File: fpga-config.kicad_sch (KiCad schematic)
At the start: 35 parts, among them J1 PinHeader_2x7_P2mm_SMD_Shroud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, Q1 BSS138PW, Q2 BSS138PW, Q3 BSS138PW, SW1 CVS-03B, SW2 SW_KMR211NGLFS_SMD, U2 TPD4E05U06QDQARQ1, U30 REF3012AIDBZT, U34 XCAU25P-2FFVB676I, U35 TMP451AIDQFR

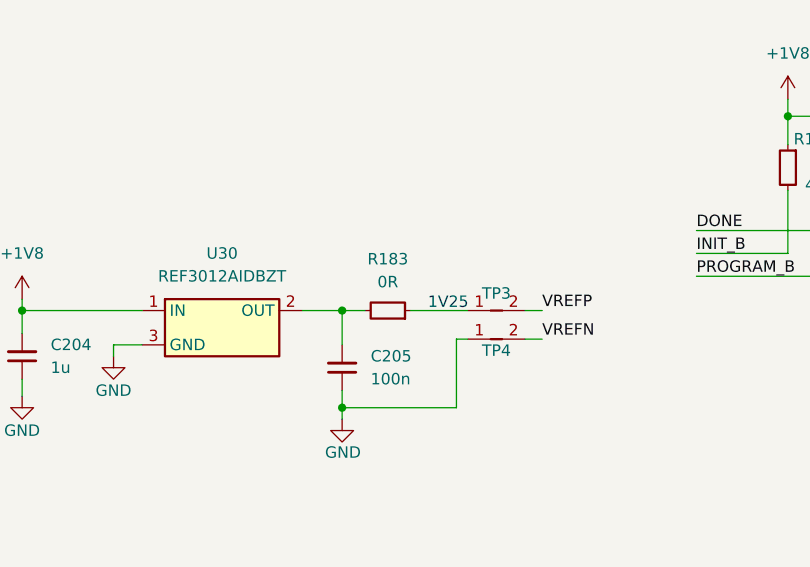
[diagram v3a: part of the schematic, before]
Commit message: [#66727] Route VCCINT sense. Route VREF. Place supply power meters circuits
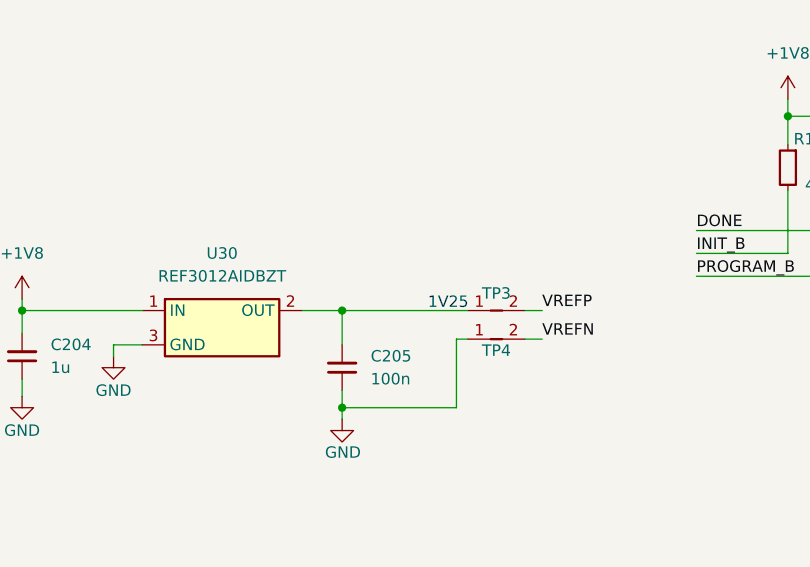
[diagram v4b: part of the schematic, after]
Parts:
- removed R183: R_0R_0402, antmicro-footprints:R_0402_1005Metric, symbol antmicroResistors0402:R_0R_0402
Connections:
- net at TP3.1: now also C205.2, U30.2 (OUT)
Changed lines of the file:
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@@
     (stroke (width 0) (type default))
   )
-  (wire (pts (xy 128.905 83.82) (xy 135.255 83.82))
+  (wire (pts (xy 121.285 83.82) (xy 135.255 83.82))
     (stroke (width 0) (type default))
   )
@@
     (stroke (width 0) (type default))
   )
-  (wire (pts (xy 121.285 83.82) (xy 123.825 83.82))
-    (stroke (width 0) (type default))
-  )
   (wire (pts (xy 29.21 229.87) (xy 29.21 232.41))
     (stroke (width 0) (type default))
@@
         )
       )
-    )
-  )
-  (symbol (lib_name "R_0R_0402_1") (lib_id "antmicroResistors0402:R_0R_0402") (at 128.905 83.82 180) (unit 1)
-    (in_bom yes) (on_board yes) (dnp no) (fields_autoplaced)
-    (property "Reference" "R183" (at 126.365 78.105 0)
-      (effects (font (size 1.27 1.27) (thickness 0.15)))
-    )
-    (property "Value" "R_0R_0402" (at 108.585 71.12 0)
-      (effects (font (size 1.27 1.27) (thickness 0.15)) (justify left bottom) hide)
-    )
-    (property "Footprint" "antmicro-footprints:R_0402_1005Metric" (at 108.585 68.58 0)
-      (effects (font (size 1.27 1.27) (thickness 0.15)) (justify left bottom) hide)
-    )
-    (property "Datasheet" "https://industrial.panasonic.com/cdbs/www-data/pdf/RDA0000/AOA0000C301.pdf" (at 108.585 66.04 0)
-      (effects (font (size 1.27 1.27) (thickness 0.15)) (justify left bottom) hide)
-    )
-    (property "MPN" "ERJ2GE0R00X" (at 108.585 63.5 0)
-      (effects (font (size 1.27 1.27) (thickness 0.15)) (justify left bottom) hide)
-    )
-    (property "Manufacturer" "Panasonic" (at 108.585 60.96 0)
-      (effects (font (size 1.27 1.27) (thickness 0.15)) (justify left bottom) hide)
-    )
-    (property "License" "Apache-2.0" (at 108.585 58.42 0)
-      (effects (font (size 1.27 1.27) (thickness 0.15)) (justify left bottom) hide)
-    )
-    (property "Author" "Antmicro" (at 108.585 55.88 0)
-      (effects (font (size 1.27 1.27) (thickness 0.15)) (justify left bottom) hide)
-    )
-    (property "Val" "0R" (at 126.365 80.645 0)
-      (effects (font (size 1.27 1.27) (thickness 0.15)))
-    )
-    (property "Tolerance" "~" (at 108.585 73.66 0)
-      (effects (font (size 1.27 1.27)) (justify left bottom) hide)
-    )
-    (property "Current" "1A" (at 108.585 53.34 0)
-      (effects (font (size 1.27 1.27) (thickness 0.15)) (justify left bottom) hide)
-    )
-    (pin "1")
-    (pin "2")
-    (instances
-      (project "data-center-rdimm-ddr5-tester"
-        (path "/1faa6543-e26a-4449-8bac-ee14b9f19e5f/00000000-0000-0000-0000-00005fd53c7d"
-          (reference "R183") (unit 1)
-        )
-      )

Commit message: [#66727] Continue routing low speed signals
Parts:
- R18: footprint antmicro-footprints:R_0402_1005Metric -> antmicro-footprints:R_0402_1005Metric_EIA
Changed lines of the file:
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@@
       (effects (font (size 1.27 1.27) (thickness 0.15)) (justify left bottom) hide)
     )
-    (property "Footprint" "antmicro-footprints:R_0402_1005Metric" (at 163.83 85.725 0)
+    (property "Footprint" "antmicro-footprints:R_0402_1005Metric_EIA" (at 163.83 85.725 0)
       (effects (font (size 1.27 1.27) (thickness 0.15)) (justify left bottom) hide)
     )

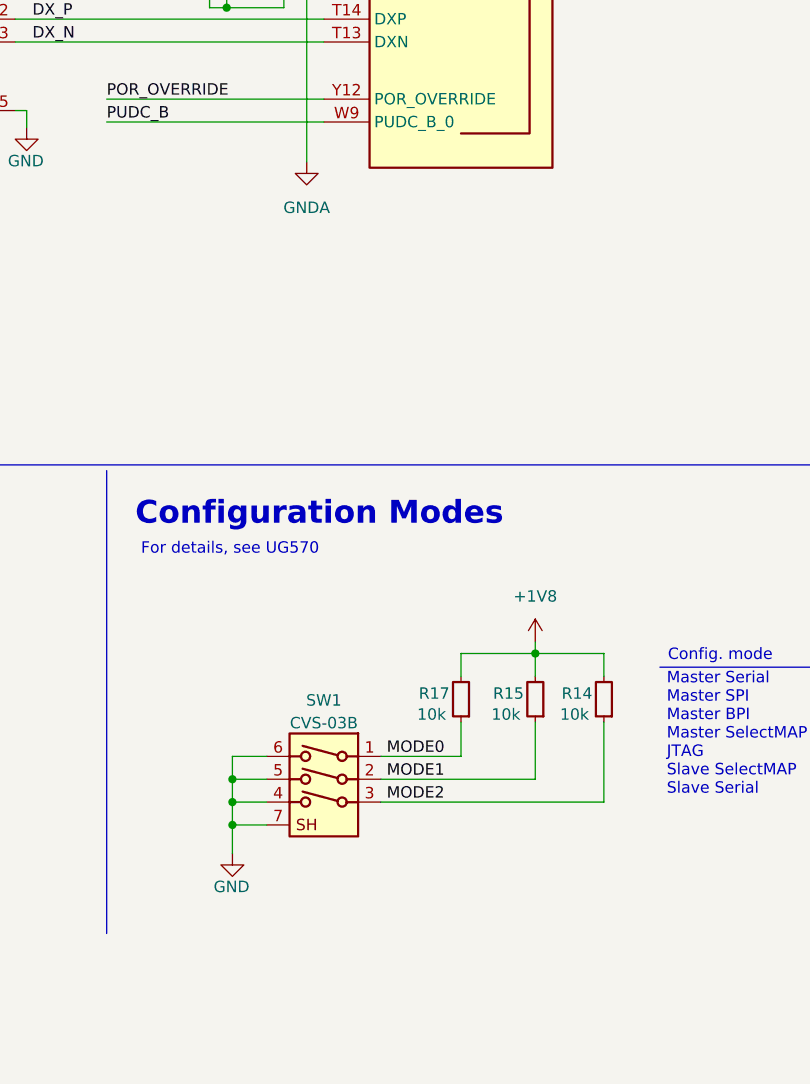
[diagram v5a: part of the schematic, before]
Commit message: [#66727] Minor schematic improvements. Finish routing right side of the board
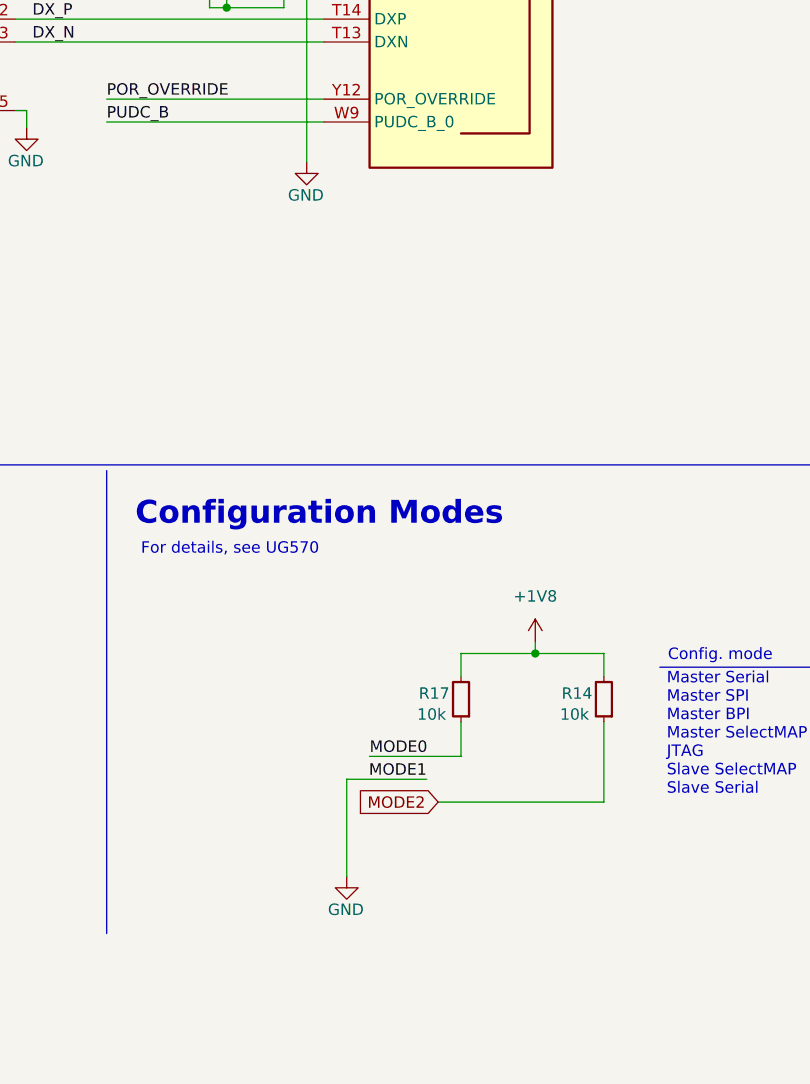
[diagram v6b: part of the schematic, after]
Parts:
- removed R15: R_10k_0402, antmicro-footprints:R_0402_1005Metric, symbol antmicroResistors0402:R_10k_0402
- removed SW1: CVS-03B, antmicro-footprints:SW_DIP_SPSTx03_Slide_Copal_CVS-03xB_W5.9mm_P1mm, symbol antmicroSlideSwitches:CVS-03B
- R14, R17: footprint antmicro-footprints:R_0402_1005Metric -> antmicro-footprints:R_0402_1005Metric_EIA
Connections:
- net GNDA is gone; now on net GND: U34.P14 (VP), U34.R13 (VN)
- net MODE1 is gone; now on net GND: U34.AA9 (M1_0)

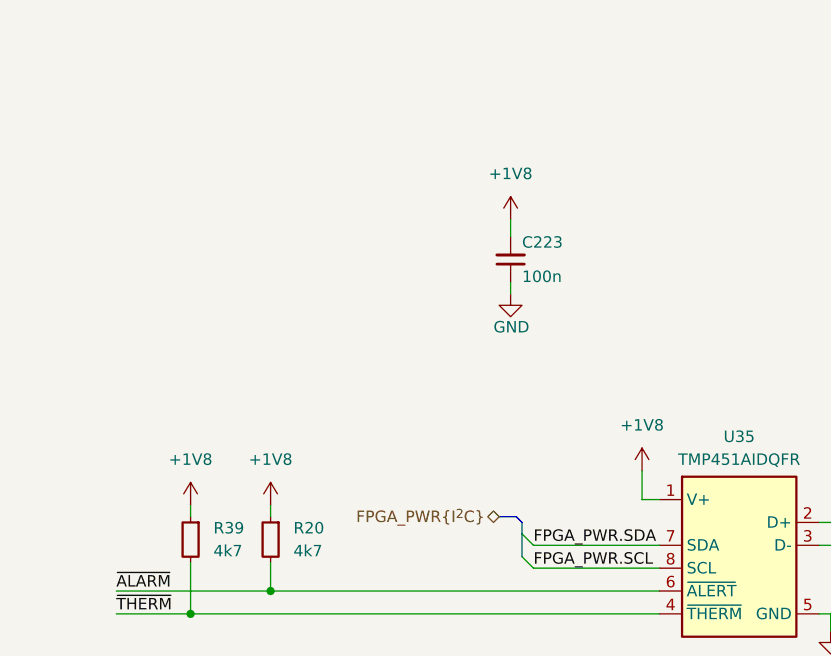
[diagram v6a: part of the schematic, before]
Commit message: [#67408] Switch TMP451AIDQFR power supply to 3V3
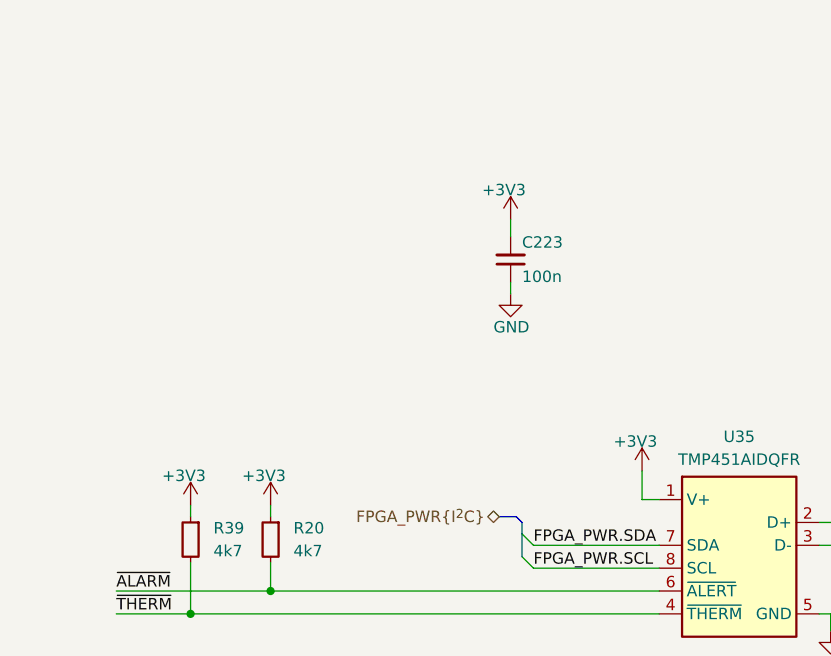
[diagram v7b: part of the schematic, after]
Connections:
- net +1V8: no longer C223.2, R20.1, R39.1, U35.1 (V+)
- net +3V3: now also C223.2, R20.1, R39.1, U35.1 (V+)

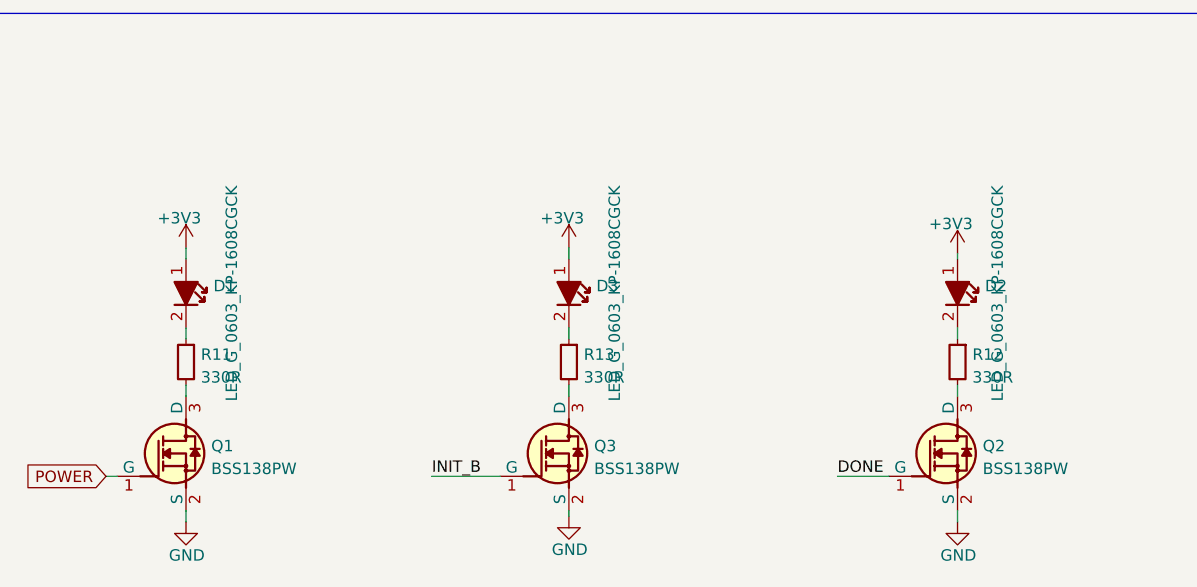
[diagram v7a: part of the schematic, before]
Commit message: [#67532] Clean DRC. Optimize power planes, EMC concept and LS/HS routing
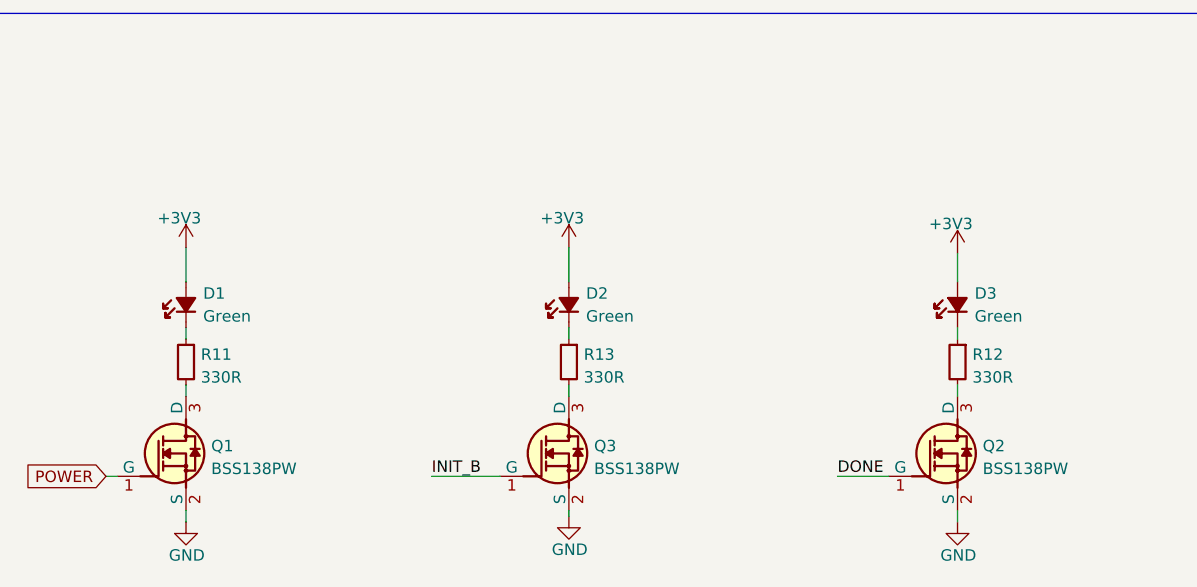
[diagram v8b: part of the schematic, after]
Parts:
- removed D1, D2, D3: LED_G_0603_KP-1608CGCK, antmicro-footprints:LED_0603_1608Metric_G, symbol antmicroLEDIndicationDiscrete:LED_G_0603_KP-1608CGCK
- added D1, D2, D3: LED_G_0402_VLMTG1500-GS08, antmicro-footprints:LED_0402_1005Metric_G, symbol antmicroLEDIndicationDiscrete:LED_G_0402_VLMTG1500-GS08
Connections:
- net +3V3: now also D1.2 (A), D2.2 (A), D3.2 (A)
- net at R12.1: now also D3.1 (C)
- net at R13.1: now also D2.1 (C)
- net at R11.1: now also D1.1 (C)
